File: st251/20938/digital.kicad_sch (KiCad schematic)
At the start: 25 parts, among them Y1 Crystal_Small, Y2 Crystal_Small

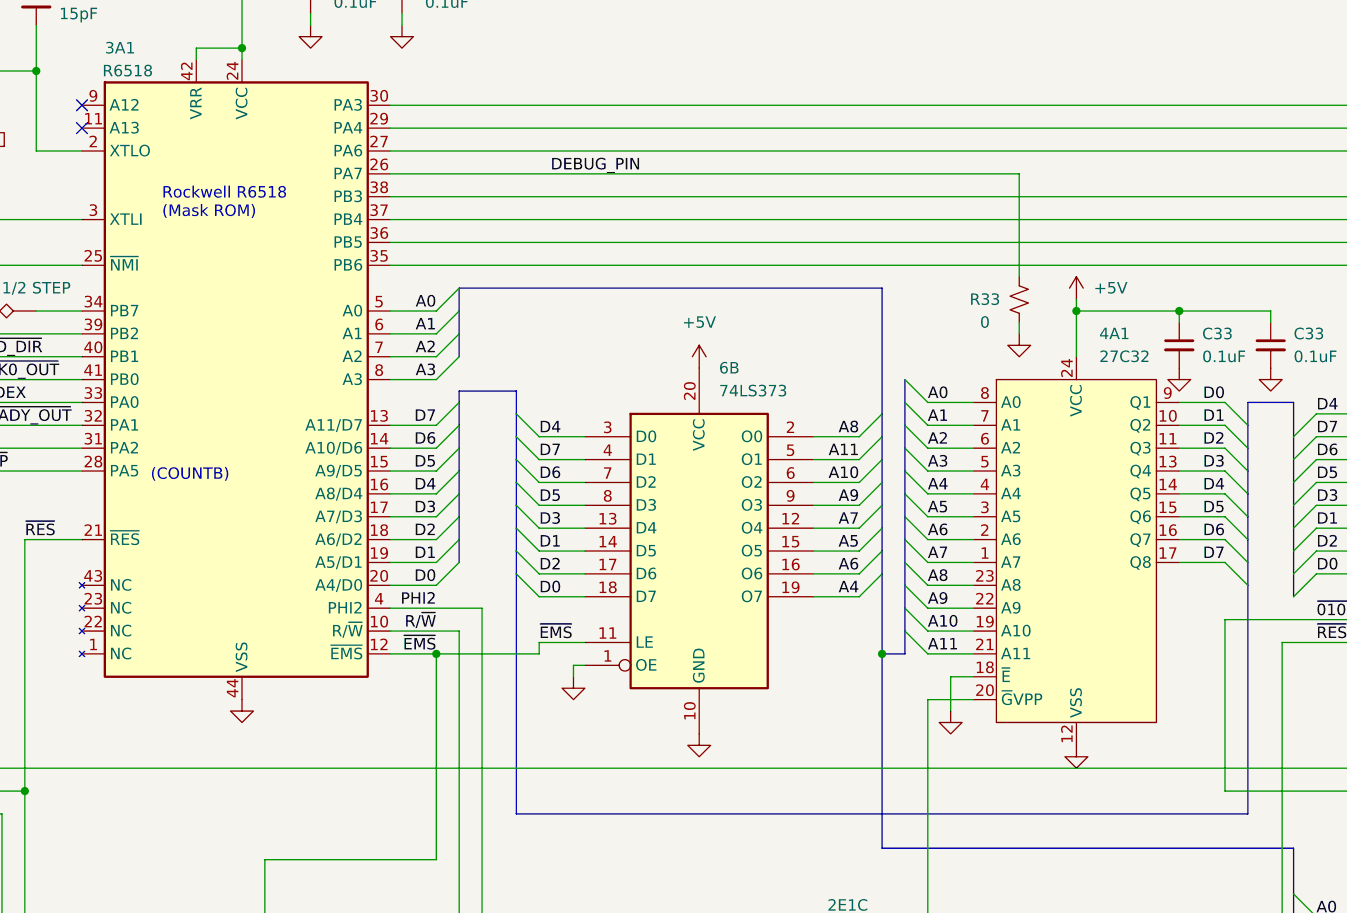
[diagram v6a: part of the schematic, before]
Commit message: Added MCU part number and stuff option for ROM
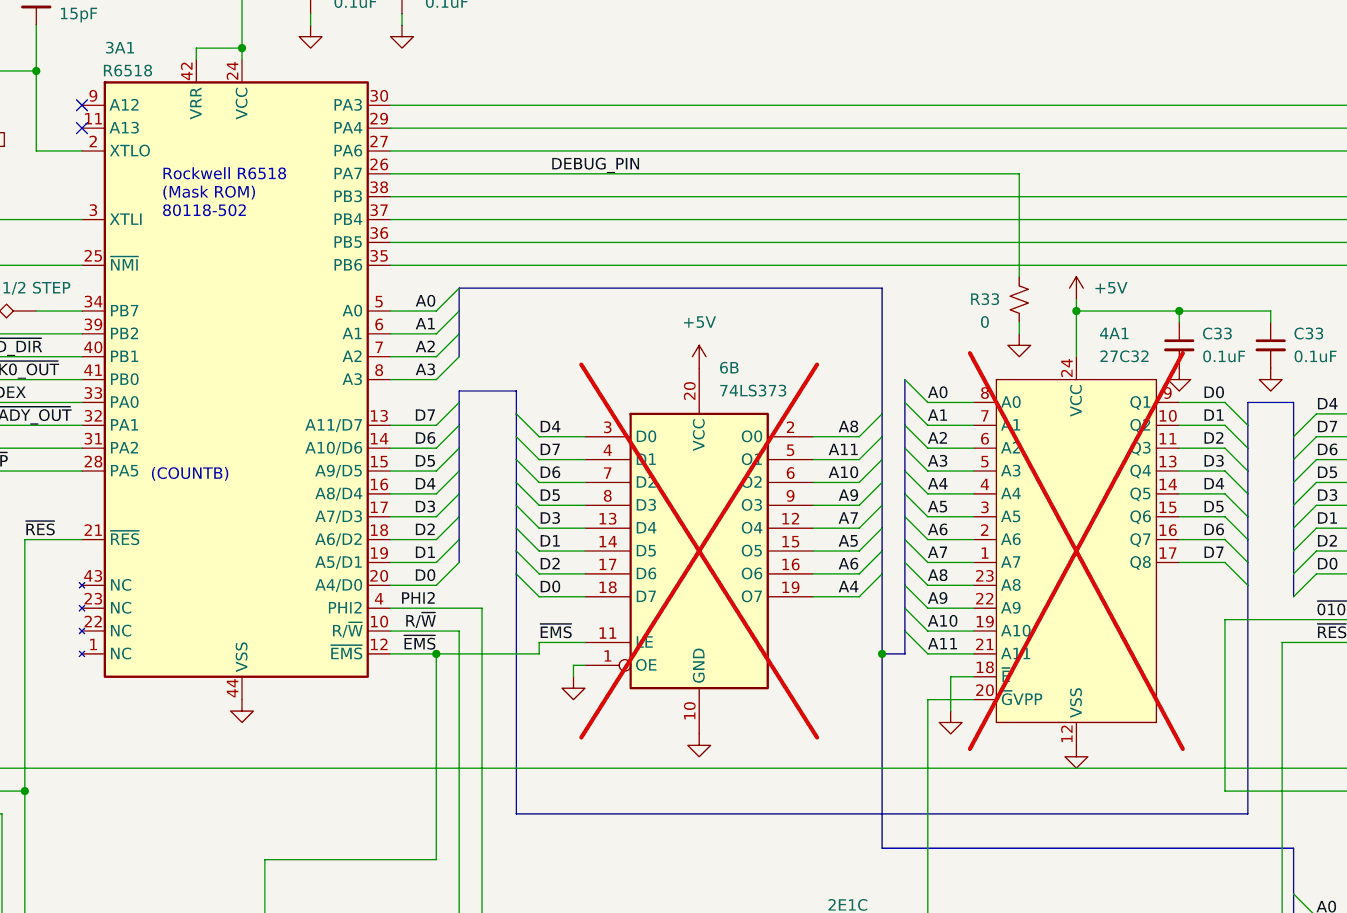
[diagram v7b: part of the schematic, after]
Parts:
- 4A1, 6B: now not fitted
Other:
- note added: "Rockwell R6518 (Mask ROM) 80118-502"
- note removed: "Rockwell R6518 (Mask ROM)"
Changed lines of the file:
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@@
     (effects (font (size 1.27 1.27)) (justify left bottom))
   )
-  (text "Rockwell R6518\n(Mask ROM)" (at 118.11 59.69 0)
+  (text "Rockwell R6518\n(Mask ROM)\n80118-502" (at 118.11 59.69 0)
     (effects (font (size 1.27 1.27)) (justify left bottom))
   )
@@
   )
   (symbol (lib_id "74xx:74LS373") (at 177.8 96.52 0) (unit 1)
-    (in_bom yes) (on_board yes) (dnp no) (fields_autoplaced)
+    (in_bom yes) (on_board yes) (dnp yes) (fields_autoplaced)
     (property "Reference" "6B" (at 179.9941 76.2 0)
       (effects (font (size 1.27 1.27)) (justify left))
@@
   )
   (symbol (lib_id "memory_new:27C32") (at 210.82 77.47 0) (unit 1)
-    (in_bom yes) (on_board yes) (dnp no)
+    (in_bom yes) (on_board yes) (dnp yes)
     (property "Reference" "4A1" (at 222.25 72.39 0)
       (effects (font (size 1.27 1.27)) (justify left))
